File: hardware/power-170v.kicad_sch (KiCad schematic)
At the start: 2 parts

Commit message: Progress point
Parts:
- removed C6: 0.1µF, Capacitor_SMD:C_0805_2012Metric, symbol Device:C
- removed D2: SMTLA5050RGB, LED_SMD:LED_WS2812B_PLCC4_5.0x5.0mm_P3.2mm, symbol LED:WS2812B
- added PS1: NCH8200HV, nch8200hv:NCH8200HV, symbol nch8200hv:NCH8200HV
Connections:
- net +5V: now also PS1.1 (VIN)
- net GND: now also PS1.2 (GND), PS1.4 (GND)
- new net +170V: PS1.3 (VOUT)

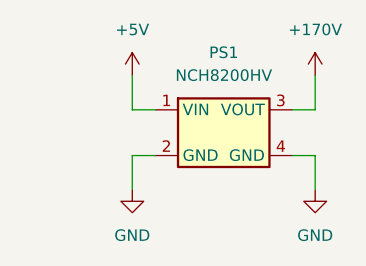
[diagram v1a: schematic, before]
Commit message: Address schematic audit findings
- Move C15 to the ESP32 EN node for proper power-on RC delay and button reset
- Add 10k boot-glitch pull-downs (R13-R16) on the CD4504 level shifter inputs
- Add NCH8200HV input capacitor (C16)
- Switch D2-D4 to the Bivar SMTLA5050RGB symbol/footprint
- Label nixie anode nets and add HV net class with custom DRC clearance rules
- Normalize value formats and assign missing footprints
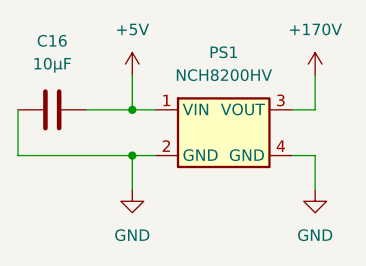
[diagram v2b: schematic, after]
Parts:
- added C16: 10µF, Capacitor_SMD:C_1206_3216Metric, symbol Device:C
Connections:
- net +5V: now also C16.1
- net GND: now also C16.2
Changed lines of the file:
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@@
 	(generator_version "10.0")
 	(paper "A4")
+	(junction
+		(at 135.89 85.09)
+		(diameter 0)
+		(color 0 0 0 0)
+	)
+	(junction
+		(at 135.89 80.01)
+		(diameter 0)
+		(color 0 0 0 0)
+	)
+	(wire
+		(pts
+			(xy 123.19 80.01) (xy 123.19 85.09)
+		)
+		(stroke
+			(width 0)
+			(type default)
+		)
+	)
 	(wire
 		(pts
@@
 	(wire
 		(pts
+			(xy 123.19 85.09) (xy 135.89 85.09)
+		)
+		(stroke
+			(width 0)
+			(type default)
+		)
+	)
+	(wire
+		(pts
 			(xy 153.67 85.09) (xy 156.21 85.09)
 		)
@@
 		(pts
 			(xy 135.89 80.01) (xy 138.43 80.01)
+		)
+		(stroke
+			(width 0)
+			(type default)
+		)
+	)
+	(wire
+		(pts
+			(xy 130.81 80.01) (xy 135.89 80.01)
 		)
 		(stroke
@@
 					(unit 1)
 				)
+			)
+		)
+	)
+	(symbol
+		(lib_id "Device:C")
+		(at 127 80.01 270)
+		(unit 1)
+		(body_style 1)
+		(exclude_from_sim no)
+		(in_bom yes)
+		(on_board yes)
+		(in_pos_files yes)
+		(dnp no)
+		(fields_autoplaced yes)
+		(property "Reference" "C16"
+			(at 127 72.39 90)
+			(show_name no)
+			(do_not_autoplace no)
+			(effects
+				(font
+					(size 1.27 1.27)
+				)
+			)
+		)
+		(property "Value" "10µF"
+			(at 127 74.93 90)
+			(show_name no)
+			(do_not_autoplace no)
+			(effects
+				(font
+					(size 1.27 1.27)
+				)
+			)
+		)
+		(property "Footprint" "Capacitor_SMD:C_1206_3216Metric"
+			(at 123.19 80.9752 0)
+			(hide yes)
+			(show_name no)
+			(do_not_autoplace no)
+			(effects
+				(font
+					(size 1.27 1.27)
+				)
+			)
+		)
+		(property "Datasheet" ""
+			(at 127 80.01 0)
+			(hide yes)
+			(show_name no)
+			(do_not_autoplace no)
+			(effects
+				(font
+					(size 1.27 1.27)
+				)
+			)
+		)
+		(property "Description" "Unpolarized capacitor"
+			(at 127 80.01 0)
+			(hide yes)
+			(show_name no)
+			(do_not_autoplace no)
+			(effects
+				(font
+					(size 1.27 1.27)
+				)
+			)
+		)
+		(pin "2"
+		)
+		(pin "1"
+		)
+		(instances
+			(project "nixie-esp32"
+				(path "/54b4b31b-75dd-48a2-8c91-a3f3099728fc/f5118c19-831d-4e27-bbb4-c31eac29ef46/5b28796d-f5fc-4c81-9d58-017f35b7ab9e"
+					(reference "C16")
+					(unit 1)
+				)

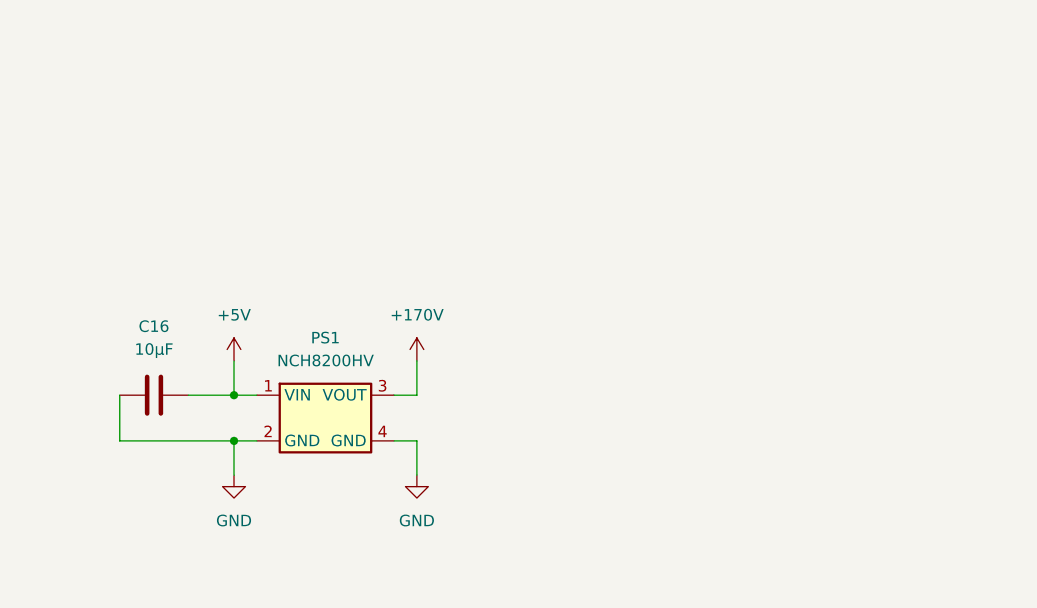
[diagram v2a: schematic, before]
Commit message: Add 5V and 170V status LED indicators
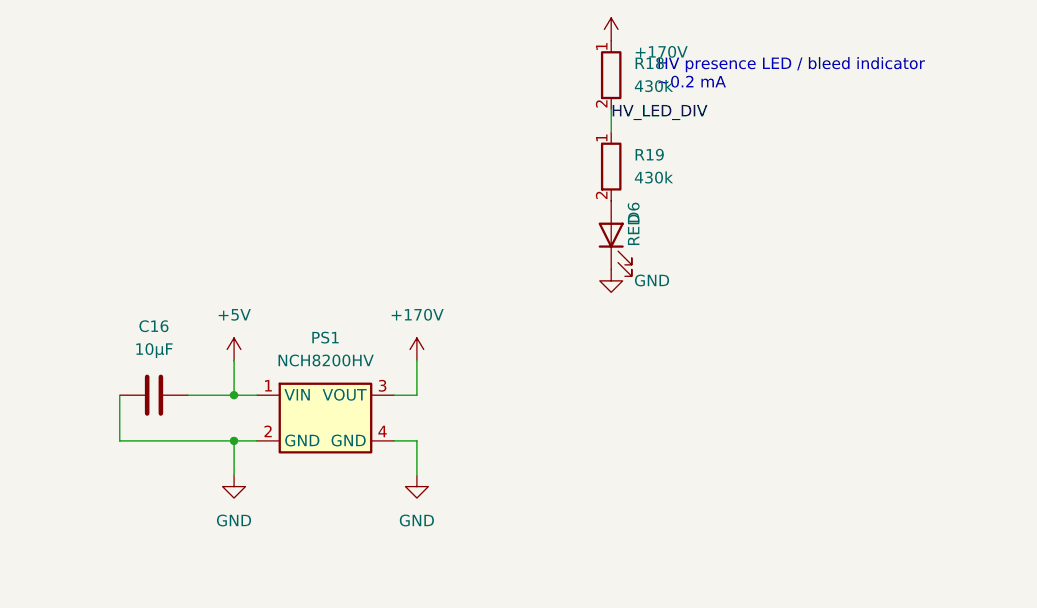
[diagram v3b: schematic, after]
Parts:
- added D6: RED, LED_SMD:LED_0805_2012Metric, symbol Device:LED
- added R18, R19: 430k, Resistor_SMD:R_0805_2012Metric, symbol Device:R
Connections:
- net +170V: now also R18.1
- net GND: now also D6.1 (K)
- new net: D6.2 (A), R19.2
- new net HV_LED_DIV: R18.2, R19.1
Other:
- note added: "HV presence LED / bleed indicator ~0.2 mA"
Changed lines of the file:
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@@
 		)
 	)
+	(symbol
+		(lib_id "nixie-esp32:+170V")
+		(at 177.8 40.64 0)
+		(unit 1)
+		(exclude_from_sim no)
+		(in_bom yes)
+		(on_board yes)
+		(dnp no)
+		(property "Reference" "#PWR071" (at 180.34 39.37 0) (effects (font (size 1.27 1.27)) (justify left) (hide yes)))
+		(property "Value" "+170V" (at 180.34 41.910000000000004 0) (effects (font (size 1.27 1.27)) (justify left)))
+		(property "Footprint" "" (at 177.8 40.64 0) (effects (font (size 1.27 1.27)) (hide yes)))
+		(property "Datasheet" "" (at 177.8 40.64 0) (effects (font (size 1.27 1.27)) (hide yes)))
+		(pin "1")
+		(instances (project "nixie-esp32" (path "/54b4b31b-75dd-48a2-8c91-a3f3099728fc/f5118c19-831d-4e27-bbb4-c31eac29ef46/5b28796d-f5fc-4c81-9d58-017f35b7ab9e" (reference "#PWR071") (unit 1))))
+	)
+	(symbol
+		(lib_id "Device:R")
+		(at 177.8 44.45 0)
+		(unit 1)
+		(exclude_from_sim no)
+		(in_bom yes)
+		(on_board yes)
+		(dnp no)
+		(property "Reference" "R18" (at 180.34 43.18 0) (effects (font (size 1.27 1.27)) (justify left)))
+		(property "Value" "430k" (at 180.34 45.720000000000006 0) (effects (font (size 1.27 1.27)) (justify left)))
+		(property "Footprint" "Resistor_SMD:R_0805_2012Metric" (at 177.8 44.45 0) (effects (font (size 1.27 1.27)) (hide yes)))
+		(property "Datasheet" "" (at 177.8 44.45 0) (effects (font (size 1.27 1.27)) (hide yes)))
+		(pin "1")
+		(pin "2")
+		(instances (project "nixie-esp32" (path "/54b4b31b-75dd-48a2-8c91-a3f3099728fc/f5118c19-831d-4e27-bbb4-c31eac29ef46/5b28796d-f5fc-4c81-9d58-017f35b7ab9e" (reference "R18") (unit 1))))
+	)
+	(symbol
+		(lib_id "Device:R")
+		(at 177.8 54.61 0)
+		(unit 1)
+		(exclude_from_sim no)
+		(in_bom yes)
+		(on_board yes)
+		(dnp no)
+		(property "Reference" "R19" (at 180.34 53.339999999999996 0) (effects (font (size 1.27 1.27)) (justify left)))
+		(property "Value" "430k" (at 180.34 55.88 0) (effects (font (size 1.27 1.27)) (justify left)))
+		(property "Footprint" "Resistor_SMD:R_0805_2012Metric" (at 177.8 54.61 0) (effects (font (size 1.27 1.27)) (hide yes)))
+		(property "Datasheet" "" (at 177.8 54.61 0) (effects (font (size 1.27 1.27)) (hide yes)))
+		(pin "1")
+		(pin "2")
+		(instances (project "nixie-esp32" (path "/54b4b31b-75dd-48a2-8c91-a3f3099728fc/f5118c19-831d-4e27-bbb4-c31eac29ef46/5b28796d-f5fc-4c81-9d58-017f35b7ab9e" (reference "R19") (unit 1))))
+	)
+	(symbol
+		(lib_id "Device:LED")
+		(at 177.8 62.23 90)
+		(unit 1)
+		(exclude_from_sim no)
+		(in_bom yes)
+		(on_board yes)
+		(dnp no)
+		(property "Reference" "D6" (at 180.34 60.959999999999994 0) (effects (font (size 1.27 1.27)) (justify left)))
+		(property "Value" "RED" (at 180.34 63.5 0) (effects (font (size 1.27 1.27)) (justify left)))
+		(property "Footprint" "LED_SMD:LED_0805_2012Metric" (at 177.8 62.23 0) (effects (font (size 1.27 1.27)) (hide yes)))
+		(property "Datasheet" "" (at 177.8 62.23 0) (effects (font (size 1.27 1.27)) (hide yes)))
+		(pin "1")
+		(pin "2")
+		(instances (project "nixie-esp32" (path "/54b4b31b-75dd-48a2-8c91-a3f3099728fc/f5118c19-831d-4e27-bbb4-c31eac29ef46/5b28796d-f5fc-4c81-9d58-017f35b7ab9e" (reference "D6") (unit 1))))
+	)
+	(symbol
+		(lib_id "power:GND")
+		(at 177.8 66.04 0)
+		(unit 1)
+		(exclude_from_sim no)
+		(in_bom yes)
+		(on_board yes)
+		(dnp no)
+		(property "Reference" "#PWR072" (at 180.34 64.77000000000001 0) (effects (font (size 1.27 1.27)) (justify left) (hide yes)))
+		(property "Value" "GND" (at 180.34 67.31 0) (effects (font (size 1.27 1.27)) (justify left)))
+		(property "Footprint" "" (at 177.8 66.04 0) (effects (font (size 1.27 1.27)) (hide yes)))
+		(property "Datasheet" "" (at 177.8 66.04 0) (effects (font (size 1.27 1.27)) (hide yes)))
+		(pin "1")
+		(instances (project "nixie-esp32" (path "/54b4b31b-75dd-48a2-8c91-a3f3099728fc/f5118c19-831d-4e27-bbb4-c31eac29ef46/5b28796d-f5fc-4c81-9d58-017f35b7ab9e" (reference "#PWR072") (unit 1))))
+	)
+	(wire (pts (xy 177.8 48.26) (xy 177.8 50.8)) (stroke (width 0) (type default)))
+	(label "HV_LED_DIV" (at 177.8 49.53 0) (effects (font (size 1.27 1.27)) (justify left bottom)))
+	(text "HV presence LED / bleed indicator\n~0.2 mA" (at 182.88 44.45 0) (effects (font (size 1.27 1.27)) (justify left)))
 )
